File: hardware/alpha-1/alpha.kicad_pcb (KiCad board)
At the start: 2 copper layers, 65 x 56 mm, 5 parts, among them P1 Conn_02x20_Odd_Even

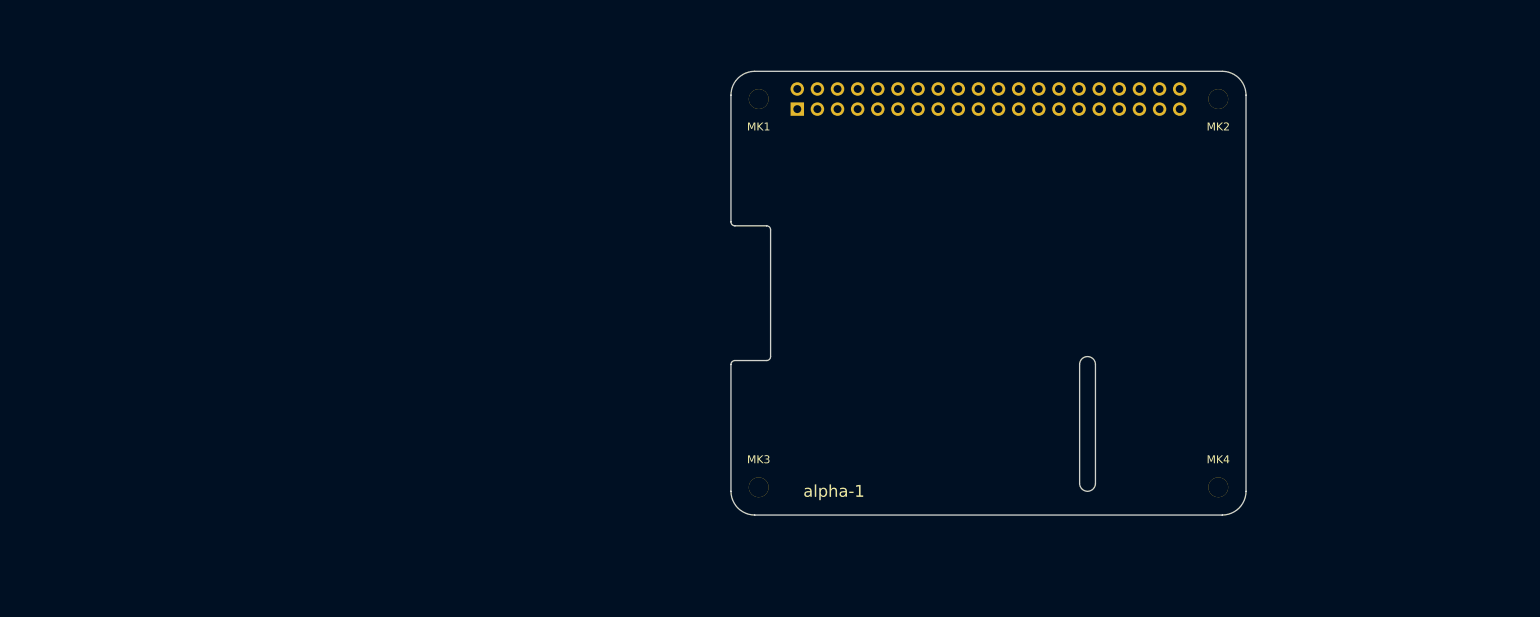
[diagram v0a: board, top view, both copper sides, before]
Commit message: o Completing all TODOs for schematic.
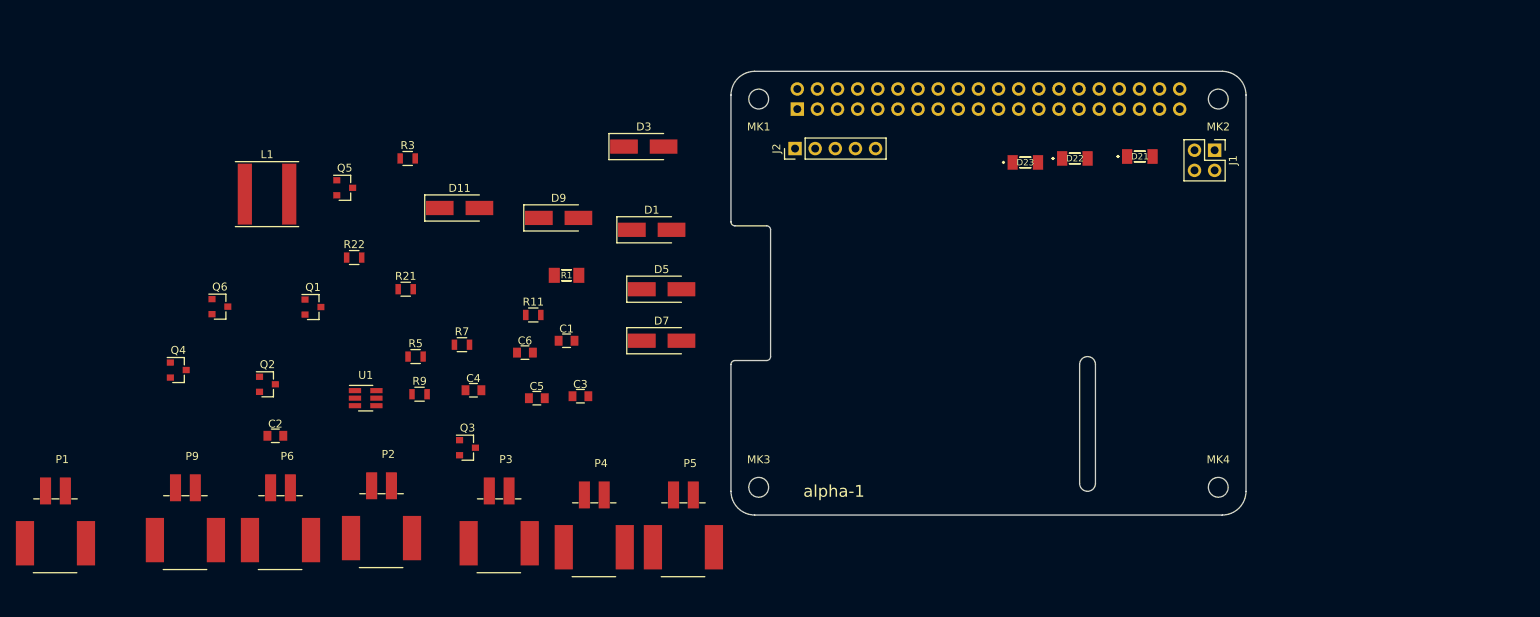
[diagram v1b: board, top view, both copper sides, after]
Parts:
- added C1: 0.1u, Capacitors_SMD:C_0805, F.Cu at (179.2, 128.0)
- added C2: 10u, Capacitors_SMD:C_0805, F.Cu at (142.5, 140.0)
- added C3: 0.1u, Capacitors_SMD:C_0805, F.Cu at (181.0, 135.0)
- added C4: 75p, Capacitors_SMD:C_0805, F.Cu at (167.5, 134.2)
- added C5: 22u, Capacitors_SMD:C_0805, F.Cu at (175.5, 135.2)
- added C6: 22u, Capacitors_SMD:C_0805, F.Cu at (174.0, 129.5)
- added D1: S1MTR, Diodes_SMD:D_SMA_Handsoldering, F.Cu at (190.0, 114.0)
- added D11: S1MTR, Diodes_SMD:D_SMA_Handsoldering, F.Cu at (165.8, 111.2)
- added D21: LED, IPC7351-Most:LEDC3216X110, F.Cu at (251.6, 104.8)
- added D22: LED, IPC7351-Most:LEDC3216X110, F.Cu at (243.4, 105.0)
- added D23: LED, IPC7351-Most:LEDC3216X110, F.Cu at (237.2, 105.5)
- added D3: S1MTR, Diodes_SMD:D_SMA_Handsoldering, F.Cu at (189.0, 103.5)
- added D5: S1MTR, Diodes_SMD:D_SMA_Handsoldering, F.Cu at (191.2, 121.5)
- added D7: S1MTR, Diodes_SMD:D_SMA_Handsoldering, F.Cu at (191.2, 128.0)
- added D9: S1MTR, Diodes_SMD:D_SMA_Handsoldering, F.Cu at (178.2, 112.5)
- added J1: POWER, Pin_Headers:Pin_Header_Straight_2x02_Pitch2.54mm, F.Cu at (261.0, 104.0)
- added J2: SERIAL, Pin_Headers:Pin_Header_Straight_1x05_Pitch2.54mm, F.Cu at (208.1, 103.8)
- added L1: 15u, Inductors_SMD:L_Taiyo-Yuden_NR-80xx, F.Cu at (141.4, 109.5)
- added P1: SWITCH_1, Bitraf:PhoenixContact_PTSM0,5_2-2,5-H_SMD, F.Cu at (114.8, 152.0)
- added P2: SWITCH_2, Bitraf:PhoenixContact_PTSM0,5_2-2,5-H_SMD, F.Cu at (155.9, 151.3)
- added P3: SWITCH_3, Bitraf:PhoenixContact_PTSM0,5_2-2,5-H_SMD, F.Cu at (170.8, 152.0)
- added P4: SWITCH_4, Bitraf:PhoenixContact_PTSM0,5_2-2,5-H_SMD, F.Cu at (182.8, 152.5)
- added P5: SWITCH_5, Bitraf:PhoenixContact_PTSM0,5_2-2,5-H_SMD, F.Cu at (194.0, 152.5)
- added P6: SWITCH_6, Bitraf:PhoenixContact_PTSM0,5_2-2,5-H_SMD, F.Cu at (143.2, 151.6)
- added P9: 12V, Bitraf:PhoenixContact_PTSM0,5_2-2,5-H_SMD, F.Cu at (131.2, 151.6)
- added Q1: DMN2041L-7, TO_SOT_Packages_SMD:SOT-23, F.Cu at (147.2, 123.8)
- added Q2: DMN2041L-7, TO_SOT_Packages_SMD:SOT-23, F.Cu at (141.5, 133.5)
- added Q3: DMN2041L-7, TO_SOT_Packages_SMD:SOT-23, F.Cu at (166.8, 141.5)
- added Q4: DMN2041L-7, TO_SOT_Packages_SMD:SOT-23, F.Cu at (130.2, 131.7)
- added Q5: DMN2041L-7, TO_SOT_Packages_SMD:SOT-23, F.Cu at (151.2, 108.7)
- added Q6: DMN2041L-7, TO_SOT_Packages_SMD:SOT-23, F.Cu at (135.5, 123.7)
- added R1: 10k, IPC7351-Most:CAPC3216X70, F.Cu at (179.2, 119.8)
- added R11: 10k, Resistors_SMD:R_0805, F.Cu at (175.1, 124.8)
- added R21: 100k, Resistors_SMD:R_0805, F.Cu at (158.9, 121.5)
- added R22: 13.3k, Resistors_SMD:R_0805, F.Cu at (152.4, 117.5)
- added R3: 10k, Resistors_SMD:R_0805, F.Cu at (159.2, 105.0)
- added R5: 10k, Resistors_SMD:R_0805, F.Cu at (160.2, 130.0)
- added R7: 10k, Resistors_SMD:R_0805, F.Cu at (166.1, 128.5)
- added R9: 10k, Resistors_SMD:R_0805, F.Cu at (160.7, 134.8)
- added U1: TPS54202, TO_SOT_Packages_SMD:SOT-23-6_Handsoldering, F.Cu at (153.9, 135.2)
- MK1, MK2, MK3, MK4: footprint Mounting_Holes:MountingHole_2-5mm -> Mounting_Holes:MountingHole_2.5mm
- P8: renamed from P1; value Conn_02x20_Odd_Even -> RASPBERRY_PI

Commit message: o Laying out all components on PCB, updating footprints. Still some parts missing.
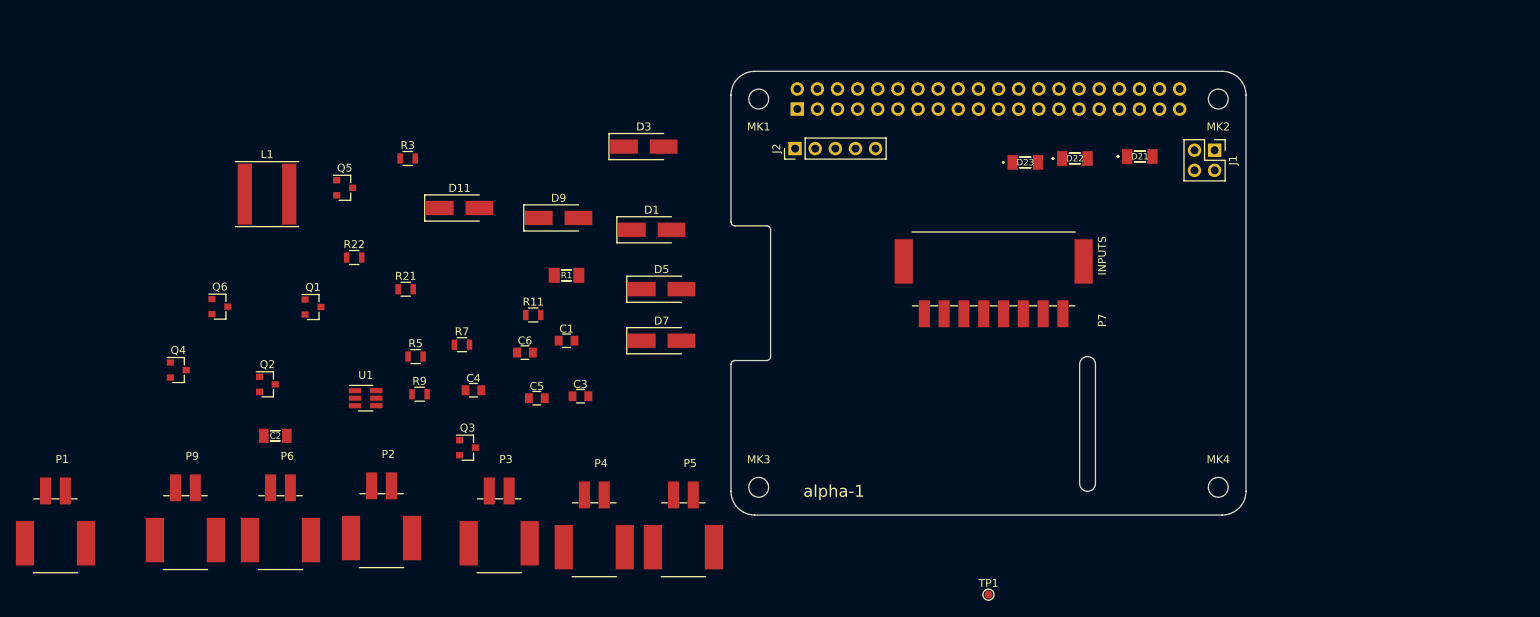
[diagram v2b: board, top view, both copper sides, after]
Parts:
- added P7: INPUTS, Bitraf:PhoenixContact_PTSM_0,5_8-2,5-H_SMD, F.Cu at (233.2, 119.6)
- added TP1: +5V, Connectors_TestPoints:Test_Point_Pad_d1.0mm, F.Cu at (232.5, 160.1)
- C2: footprint Capacitors_SMD:C_0805 -> IPC7351-Nominal:CAPC3216X70
- P1, P2, P3, P4, P5, P6, P9: footprint Bitraf:PhoenixContact_PTSM0,5_2-2,5-H_SMD -> Bitraf:PhoenixContact_PTSM_0,5_2-2,5-H_SMD
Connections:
- C2 pad 1: Vin -> +12V
- C3 pad 1: Vin -> +12V
- P9 pad 1: Vin -> +12V
- U1 pad 3: Vin -> +12V

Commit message: o Refactoring schematic, moving inputs to the left, outputs to the right and the header in the middle.
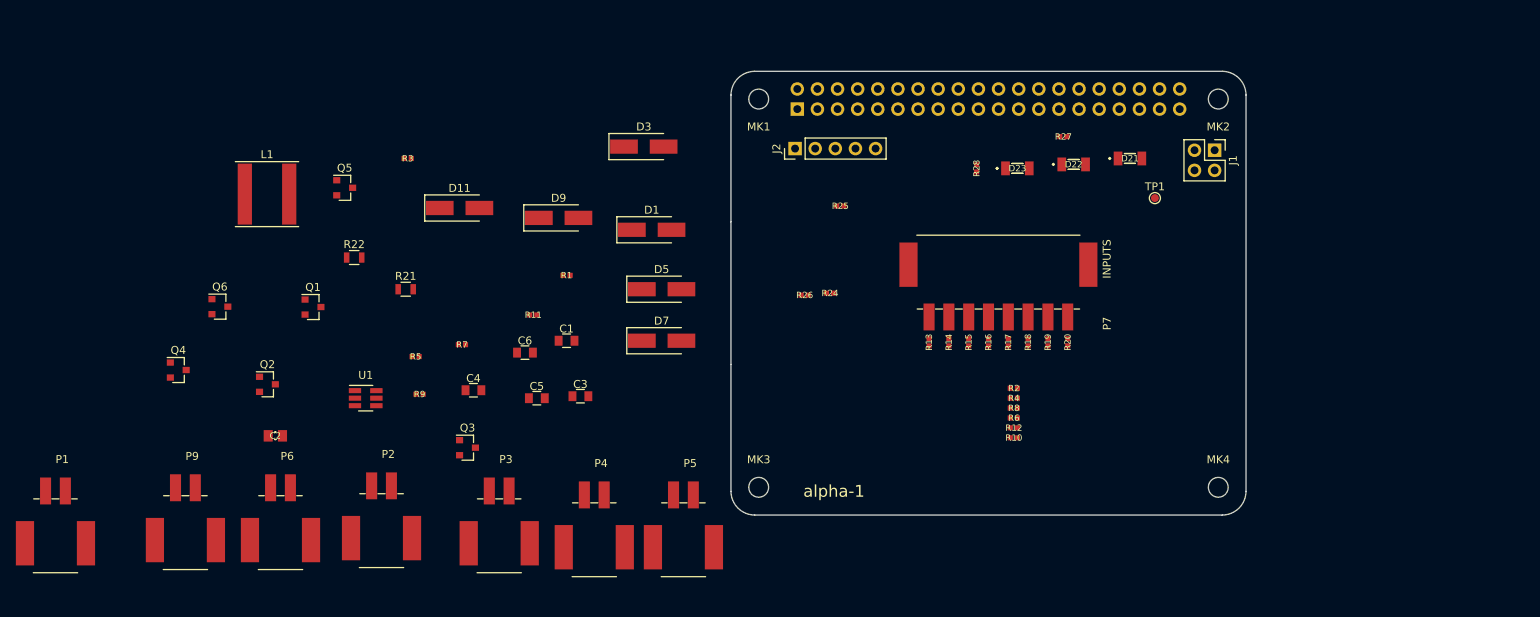
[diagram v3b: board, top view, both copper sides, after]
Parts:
- added R10: 270, IPC7351-Nominal:RESC1005X38, F.Cu at (235.7, 140.2)
- added R12: 270, IPC7351-Nominal:RESC1005X38, F.Cu at (235.7, 139.0)
- added R13: 10k, IPC7351-Nominal:RESC1005X38, F.Cu at (225.0, 128.2)
- added R14: 10k, IPC7351-Nominal:RESC1005X38, F.Cu at (227.5, 128.2)
- added R15: 10k, IPC7351-Nominal:RESC1005X38, F.Cu at (230.0, 128.2)
- added R16: 10k, IPC7351-Nominal:RESC1005X38, F.Cu at (232.5, 128.2)
- added R17: 10k, IPC7351-Nominal:RESC1005X38, F.Cu at (235.0, 128.2)
- added R18: 10k, IPC7351-Nominal:RESC1005X38, F.Cu at (237.5, 128.2)
- added R19: 10k, IPC7351-Nominal:RESC1005X38, F.Cu at (240.0, 128.2)
- added R2: 270, IPC7351-Nominal:RESC1005X38, F.Cu at (235.7, 134.0)
- added R20: 10k, IPC7351-Nominal:RESC1005X38, F.Cu at (242.5, 128.2)
- added R24: 10k, IPC7351-Nominal:RESC1005X38, F.Cu at (212.5, 122.0)
- added R25: 10k, IPC7351-Nominal:RESC1005X38, F.Cu at (213.8, 111.0)
- added R26: 10k, IPC7351-Nominal:RESC1005X38, F.Cu at (209.3, 122.2)
- added R27: 560, IPC7351-Nominal:RESC1005X38, F.Cu at (241.9, 102.2)
- added R28: 560, IPC7351-Nominal:RESC1005X38, F.Cu at (231.0, 106.2)
- added R4: 270, IPC7351-Nominal:RESC1005X38, F.Cu at (235.7, 135.2)
- added R6: 270, IPC7351-Nominal:RESC1005X38, F.Cu at (235.7, 137.8)
- added R8: 270, IPC7351-Nominal:RESC1005X38, F.Cu at (235.7, 136.5)
- C2: footprint IPC7351-Nominal:CAPC3216X70 -> IPC7351-Nominal:CAPC2012X70
- D21, D22, D23: footprint IPC7351-Most:LEDC3216X110 -> IPC7351-Nominal:LEDC3216X110
- R1: footprint IPC7351-Most:CAPC3216X70 -> IPC7351-Nominal:RESC1005X38
- R11, R3, R5, R7, R9: footprint Resistors_SMD:R_0805 -> IPC7351-Nominal:RESC1005X38
- moved TP1 54.3 mm to (253.5, 110.0)
- moved D21 1.27 mm to (250.3, 105.0)
- moved D23 1.25 mm to (236.2, 106.2)
- moved D22 0.76 mm to (243.2, 105.8)
- moved P7 0.72 mm to (233.8, 120.0)
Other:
- outline, holes or cut-outs redrawn

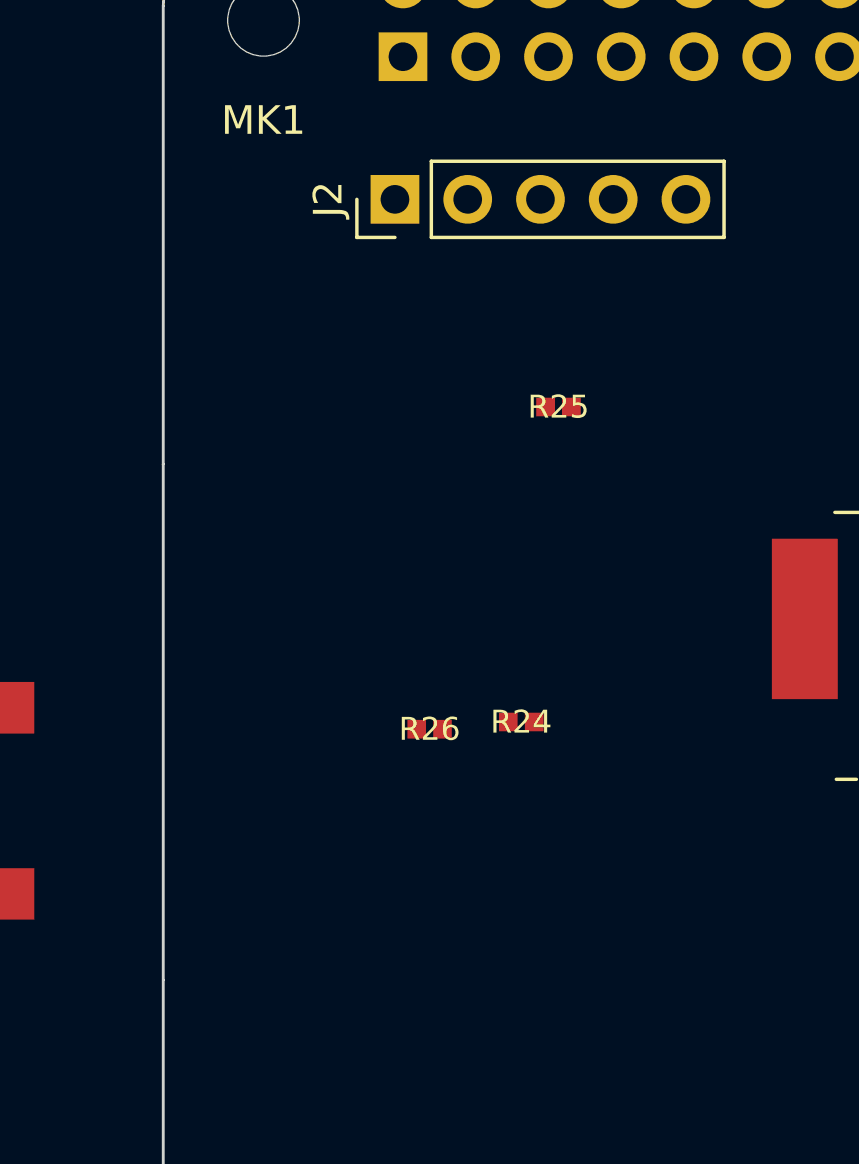
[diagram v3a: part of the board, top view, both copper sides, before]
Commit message: o Footprints should be complete, still missing some MPNs.
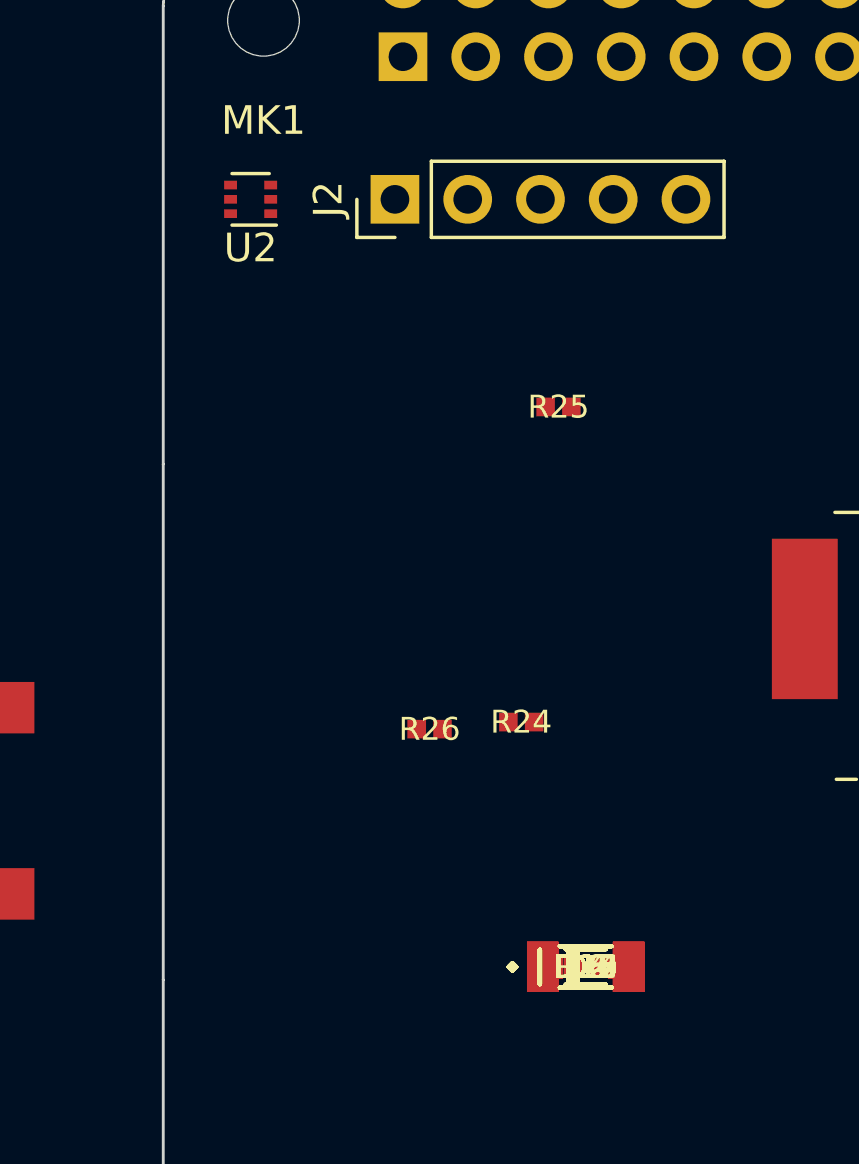
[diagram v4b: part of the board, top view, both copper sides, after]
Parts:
- added D10, D12, D2, D4, D6, D8: LED, IPC7351-Nominal:LEDC3216X110, F.Cu at (214.8, 130.6)
- added D13, D14, D15, D16, D17, D18, D19, D20: BZX384C4V7, smd-semi:SOD-323, F.Cu at (214.8, 130.6)
- added R23: 560, IPC7351-Nominal:RESC1005X38, F.Cu at (214.8, 130.6)
- added U2: TMP102, Bitraf:SOT-553, F.Cu at (203.1, 103.8)
